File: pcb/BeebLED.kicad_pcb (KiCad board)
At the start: 2 copper layers, 55.9 x 65.5 mm, 14 parts, among them J1 BBC User Port, J2 Jack-DC, J3 WS51282B, U1 74HC14, U2 74LS165, X1 8Mhz, X2 8Mhz

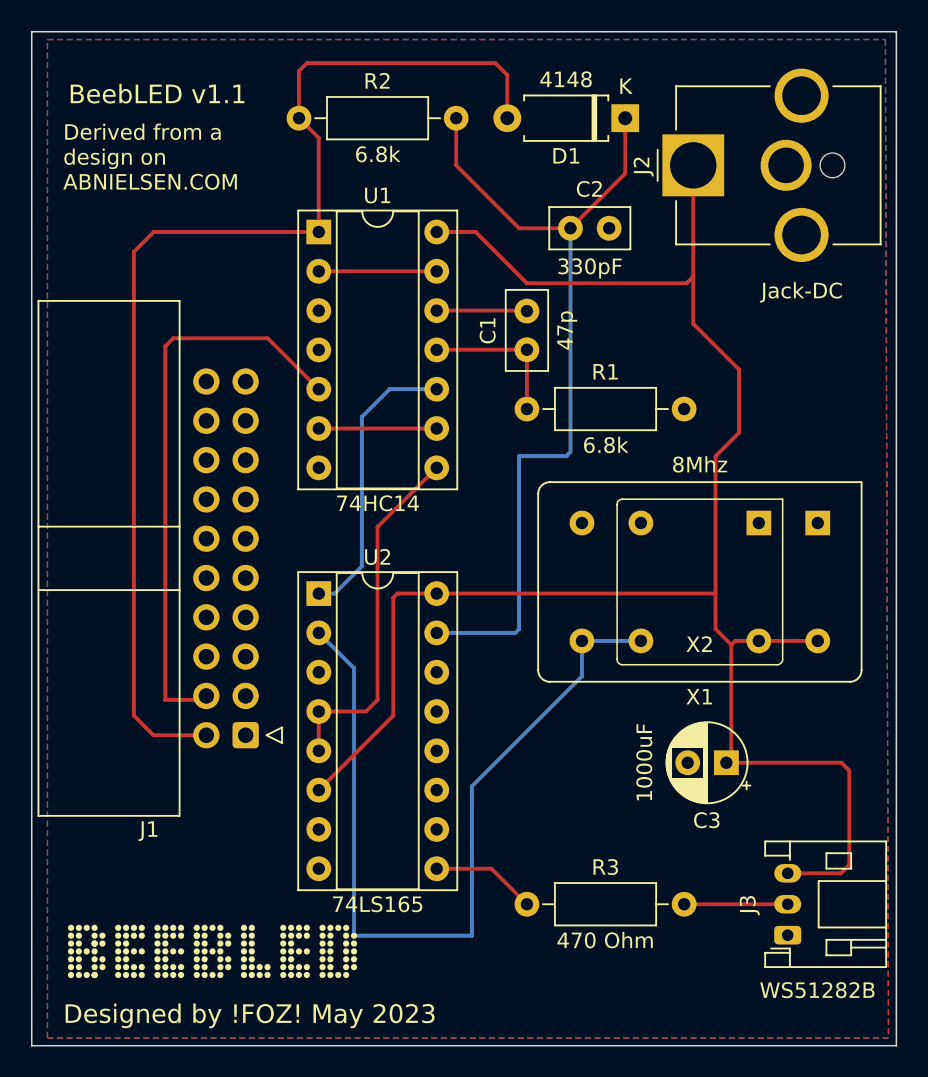
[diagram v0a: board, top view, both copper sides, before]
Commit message: Updated to v1.2 schematic and pcb design
Requires further testing
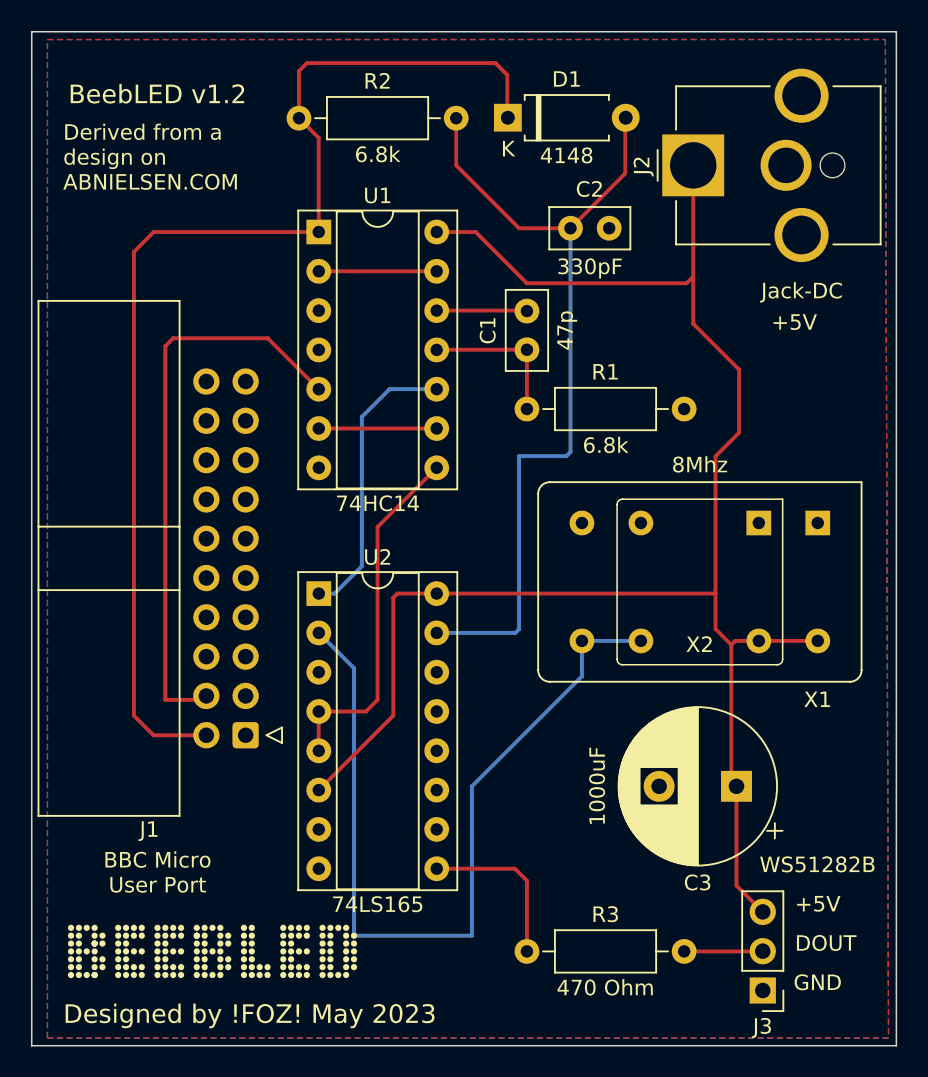
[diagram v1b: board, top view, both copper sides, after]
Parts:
- C3: footprint Capacitor_THT:CP_Radial_D5.0mm_P2.50mm -> Capacitor_THT:CP_Radial_D10.0mm_P5.00mm
- J1: value BBC User Port -> BBC Micro User Port
- J3: footprint Connector_JST:JST_PH_S3B-PH-K_1x03_P2.00mm_Horizontal -> Connector_PinHeader_2.54mm:PinHeader_1x03_P2.54mm_Vertical
- moved D1 7.58 mm to (111.5, 41.6), turned to 0 degrees
- moved J3 3.92 mm to (128.0, 98.0), turned to 180 degrees
- moved R3 3.05 mm to (112.8, 95.5)
- moved C3 1.66 mm to (126.3, 84.8)
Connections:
- D1 pad 1: Net-(C2-Pad1) -> Net-(D1-Pad1)
- D1 pad 2: Net-(D1-Pad2) -> Net-(C2-Pad1)
- J1 pad 2: Net-(D1-Pad2) -> Net-(D1-Pad1)
- R2 pad 1: Net-(D1-Pad2) -> Net-(D1-Pad1)
- U1 pad 1: Net-(D1-Pad2) -> Net-(D1-Pad1)
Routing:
- net Net-(D1-Pad2): track 75.4 -> 0.00 mm
- net Net-(D1-Pad1): track 0.00 -> 75.4 mm
- net +5V: track 119.3 -> 110.6 mm
- net Net-(R3-Pad1): track 6.78 -> 10.2 mm
- net Net-(J3-Pad2): track 6.69 -> 5.09 mm
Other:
- board text added: "+5V"
- board text added: "BBC Micro User Port"
- board text added: "BeebLED v1.2"
- board text added: "DOUT"
- board text added: "GND"
- board text removed: "BeebLED v1.1"
